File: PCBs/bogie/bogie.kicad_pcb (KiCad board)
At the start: 2 copper layers, 56.5 x 78 mm, 7 parts

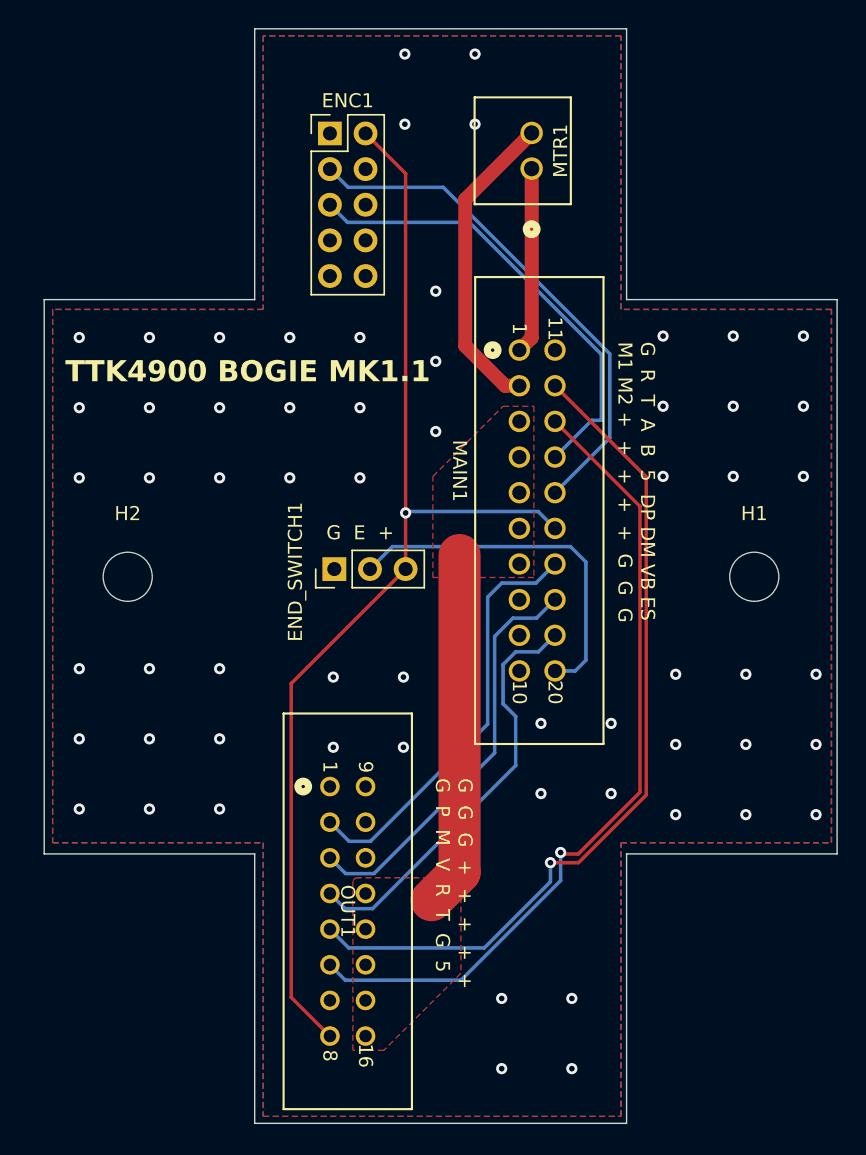
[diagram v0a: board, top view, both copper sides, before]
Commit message: Working UART input for basic control. All motors work. Next up: switch interrupts
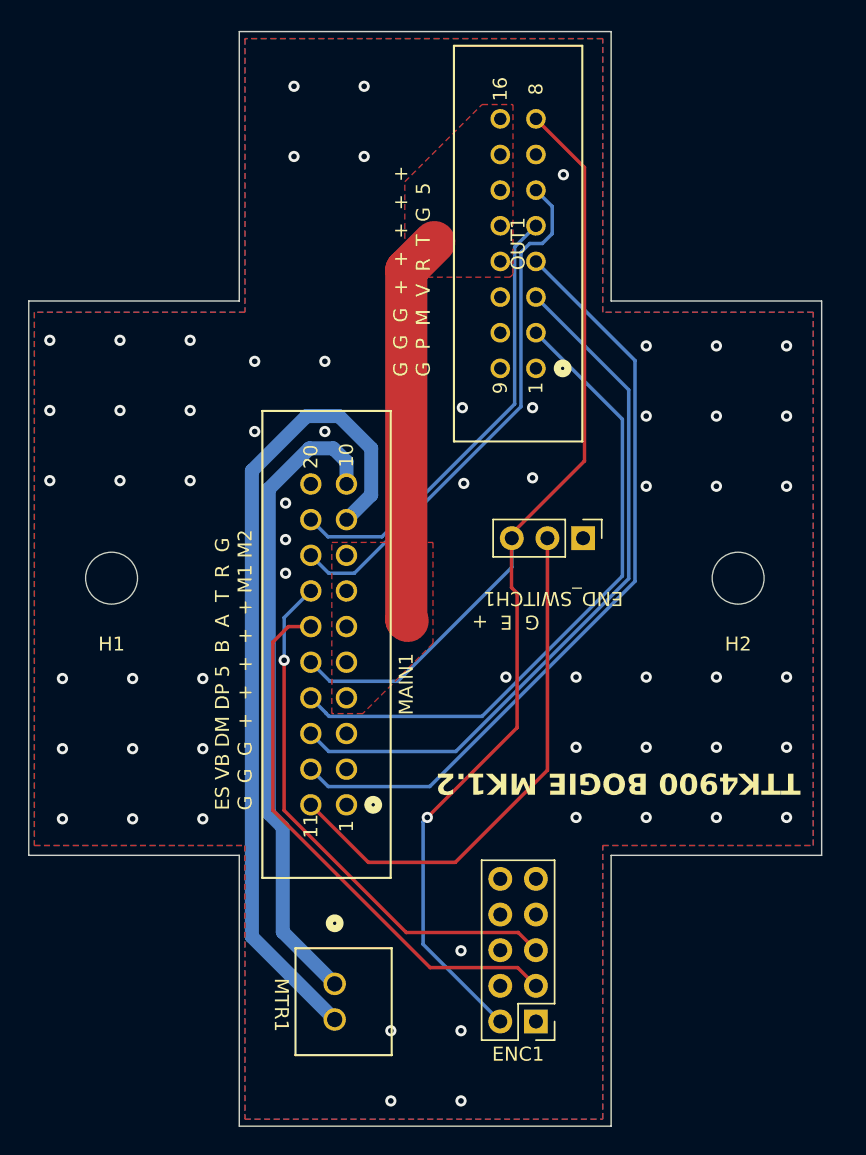
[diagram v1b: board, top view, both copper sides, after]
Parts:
- H1, H2: footprint MountingHole:MountingHole_3.5mm -> MountingHole:MountingHole_3.7mm
- moved ENC1 65.0 mm to (108.9, 91.2), turned to 180 degrees
- moved MTR1 59.8 mm to (94.6, 88.6), turned to -90 degrees
- moved H1 45.8 mm to (78.7, 59.6), turned to 180 degrees
- moved H2 43.5 mm to (123.3, 59.6), turned to 180 degrees
- moved MAIN1 34.7 mm to (95.4, 75.8), turned to 90 degrees
- moved OUT1 33.2 mm to (108.9, 44.7), turned to 90 degrees
- moved END_SWITCH1 17.9 mm to (112.3, 56.8), turned to -90 degrees
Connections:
- MAIN1 pad 1: /MTR1_IN -> GND
- MAIN1 pad 10: GND -> /MTR1_IN
- MAIN1 pad 11: GND -> /END_SWITCH
- MAIN1 pad 12: /UART_RX -> /VB_OUT
- MAIN1 pad 13: /UART_TX -> /DM_OUT
- MAIN1 pad 14: /ENC1B -> /DP_OUT
- MAIN1 pad 15: /ENC1A -> +5V
- MAIN1 pad 16: +5V -> /ENC1A
- MAIN1 pad 17: /DP_OUT -> /ENC1B
- MAIN1 pad 18: /DM_OUT -> /UART_TX
- MAIN1 pad 19: /VB_OUT -> /UART_RX
- MAIN1 pad 2: /MTR1_OUT -> GND
- MAIN1 pad 20: /END_SWITCH -> GND
- MAIN1 pad 3: +48V -> GND
- MAIN1 pad 8: GND -> +48V
- MAIN1 pad 9: GND -> /MTR1_OUT
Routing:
- net /MTR1_OUT: track 22.2 -> 58.4 mm
- net /MTR1_IN: track 13.3 -> 45.9 mm
- net /UART_RX: track 60.3 -> 32.3 mm, vias 1 -> 0
- net /VB_OUT: track 30.0 -> 55.4 mm
- net /DM_OUT: track 29.5 -> 51.1 mm
- net /UART_TX: track 58.3 -> 37.8 mm, vias 1 -> 0
- net /DP_OUT: track 30.1 -> 46.8 mm
- net +5V: track 81.2 -> 93.5 mm
- net /END_SWITCH: track 26.0 -> 37.8 mm
- net /ENC1B: track 32.8 -> 38.5 mm, vias 0 -> 1
- net +48V: track 25.4 -> 27.9 mm
- net /ENC1A: track 36.9 -> 39.1 mm
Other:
- outline, holes or cut-outs redrawn
- board text added: "ES VB DM DP 5 B A T R G G G G + + + + + M1 M2"
- board text added: "TTK4900 BOGIE MK1.2"
- board text removed: "G R T A B 5 DP DM VB ES M1 M2 + + + + + G G G"
- board text removed: "TTK4900 BOGIE MK1.1"
